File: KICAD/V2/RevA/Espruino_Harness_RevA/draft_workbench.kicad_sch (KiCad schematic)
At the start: 0 parts

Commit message: Implement Target Interface and GPIO loopback
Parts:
- added J900: TARGET INTERFACE CONNECTOR A, symbol Espruino_Harness_RevA:Target_Interface_2x12_Odd_Even
- added J901: TARGET INTERFACE CONNECTOR B, symbol Espruino_Harness_RevA:Target_Interface_2x12_Odd_Even
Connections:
- new net R0: J900.3 (Contact_03)
- new net R1: J900.4 (Contact_04)
- new net R2: J900.5 (Contact_05)
- new net R3: J900.6 (Contact_06)
- new net R4: J900.7 (Contact_07)
- new net R5: J900.9 (Contact_09)
- new net R6: J900.10 (Contact_10)
- new net TI_ANALOG_ADC_IN: J900.22 (Contact_22)
- new net TI_ANALOG_PWM_OUT: J900.21 (Contact_21)
- new net TI_BOOT_REQUEST: J900.13 (Contact_13)
- new net TI_GND: J900.12 (Contact_12), J900.16 (Contact_16), J900.2 (Contact_02), J900.20 (Contact_20), J900.24 (Contact_24), J900.8 (Contact_08), J901.12 (Contact_12), J901.16 (Contact_16), J901.2 (Contact_02), J901.20 (Contact_20), J901.24 (Contact_24), J901.8 (Contact_08)
- new net TI_GPIO_LOOP_A_IN: J901.4 (Contact_04)
- new net TI_GPIO_LOOP_A_OUT: J901.3 (Contact_03)
- new net TI_GPIO_LOOP_B_IN: J901.6 (Contact_06)
- new net TI_GPIO_LOOP_B_OUT: J901.5 (Contact_05)
- new net TI_I2C_FB: J900.18 (Contact_18)
- new net TI_I2C_INT: J900.19 (Contact_19)
- new net TI_I2C_SCL: J900.17 (Contact_17)
- new net TI_I2C_SDA: J900.15 (Contact_15)
- new net TI_ONEWIRE_DQ: J901.14 (Contact_14)
- new net TI_ONEWIRE_GPIO_A_FB: J901.15 (Contact_15)
- new net TI_ONEWIRE_GPIO_B_FB: J901.17 (Contact_17)
- new net TI_RGB_DATA: J900.14 (Contact_14)
- new net TI_SPI_CS_ADC: J901.11 (Contact_11)
- new net TI_SPI_CS_EXT: J901.13 (Contact_13)
- new net TI_SPI_MISO: J901.10 (Contact_10)
- new net TI_SPI_MOSI: J901.9 (Contact_09)
- new net TI_SPI_SCK: J901.7 (Contact_07)
- new net TI_SWITCHED_TARGET_5V: J900.23 (Contact_23), J901.23 (Contact_23)
- new net TI_TARGET_3V3: J900.1 (Contact_01), J901.1 (Contact_01)
- new net TI_TARGET_RESET_N: J900.11 (Contact_11)
- new net TI_UART_A_RX: J901.19 (Contact_19)
- new net TI_UART_A_TX: J901.18 (Contact_18)
- new net TI_UART_B_RX: J901.22 (Contact_22)
- new net TI_UART_B_TX: J901.21 (Contact_21)

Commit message: Implement V2 routing fabric and control
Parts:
- added C610, C611: 100nF, Capacitor_SMD:C_0603_1608Metric, symbol Device:C
- added JP610: A0 default 1, Jumper:SolderJumper-3_P1.3mm_Bridged12_RoundedPad1.0x1.5mm_NumberLabels, symbol Jumper:SolderJumper_3_Bridged12
- added JP611: A1 default 0, Jumper:SolderJumper-3_P1.3mm_Bridged12_RoundedPad1.0x1.5mm_NumberLabels, symbol Jumper:SolderJumper_3_Bridged12
- added JP612, JP615: A2 default 0, Jumper:SolderJumper-3_P1.3mm_Bridged12_RoundedPad1.0x1.5mm_NumberLabels, symbol Jumper:SolderJumper_3_Bridged12
- added JP613: A0 default 0, Jumper:SolderJumper-3_P1.3mm_Bridged12_RoundedPad1.0x1.5mm_NumberLabels, symbol Jumper:SolderJumper_3_Bridged12
- added JP614: A1 default 1, Jumper:SolderJumper-3_P1.3mm_Bridged12_RoundedPad1.0x1.5mm_NumberLabels, symbol Jumper:SolderJumper_3_Bridged12
- added U610: MCP23017-E/SO RCTRL0, Package_SO:SOIC-28W_7.5x17.9mm_P1.27mm, symbol Espruino_Harness_RevA:MCP23017_SO
- added U611: MCP23017-E/SO RCTRL1, Package_SO:SOIC-28W_7.5x17.9mm_P1.27mm, symbol Espruino_Harness_RevA:MCP23017_SO
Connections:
- net TI_GND: now also C610.2, C611.2, JP610.3 (B), JP611.1 (A), JP612.1 (A), JP613.1 (A), JP614.3 (B), JP615.1 (A), U610.10 (VSS), U611.10 (VSS)
- new net: JP612.2 (C), U610.17 (A2)
- new net: JP615.2 (C), U611.17 (A2)
- new net: JP611.2 (C), U610.16 (A1)
- new net: JP614.2 (C), U611.16 (A1)
- new net: JP610.2 (C), U610.15 (A0)
- new net: JP613.2 (C), U611.15 (A0)
- new net ROUTE_CLEAR_N: U610.18 (~{RESET}), U611.18 (~{RESET})
- new net ROUTE_I2C_SCL: U610.12 (SCL), U611.12 (SCL)
- new net ROUTE_I2C_SDA: U610.13 (SDA), U611.13 (SDA)
- new net ROUTING_LOGIC_3V3: C610.1, C611.1, JP610.1 (A), JP611.3 (B), JP612.3 (B), JP613.3 (B), JP614.1 (A), JP615.3 (B), U610.9 (VDD), U611.9 (VDD)
- new net RP01_EN: U610.21 (GPA0)
- new net RP02_EN: U610.22 (GPA1)
- new net RP03_EN: U610.23 (GPA2)
- new net RP04_EN: U610.24 (GPA3)
- new net RP05_EN: U610.25 (GPA4)
- new net RP06_EN: U610.26 (GPA5)
- new net RP07_EN: U610.27 (GPA6)
- new net RP08_EN: U610.28 (GPA7)
- new net RP09_EN: U610.1 (GPB0)
- new net RP10_EN: U610.2 (GPB1)
- new net RP11_EN: U610.3 (GPB2)
- new net RP12_EN: U610.4 (GPB3)
- new net RP13_EN: U610.5 (GPB4)
- new net RP14_EN: U610.6 (GPB5)
- new net RP15_EN: U610.7 (GPB6)
- new net RP16_EN: U610.8 (GPB7)
- new net RP17_EN: U611.21 (GPA0)
- new net RP18_EN: U611.22 (GPA1)
- new net RP19_EN: U611.23 (GPA2)
- new net UP01_EN: U611.24 (GPA3)
- new net UP02_EN: U611.25 (GPA4)
- new net UP03_EN: U611.26 (GPA5)
- new net UP04_EN: U611.27 (GPA6)
- no-connect marks 0 -> 13
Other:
- note added: "Address selectors: pads 1-2 are default; to change, cut 1-2 and bridge 2-3. Never bridge both."
- note added: "Both controllers share ROUTE_I2C_SDA / ROUTE_I2C_SCL and active-low ROUTE_CLEAR_N"
- note added: "ROUTING CONTROLLER DRAFT â€” REVIEW BEFORE COPYING TO PRODUCTION"
- note added: "U610 â€” RCTRL0 â€” MCP23017 address 0x21"
- note added: "U611 â€” RCTRL1 â€” MCP23017 address 0x22"

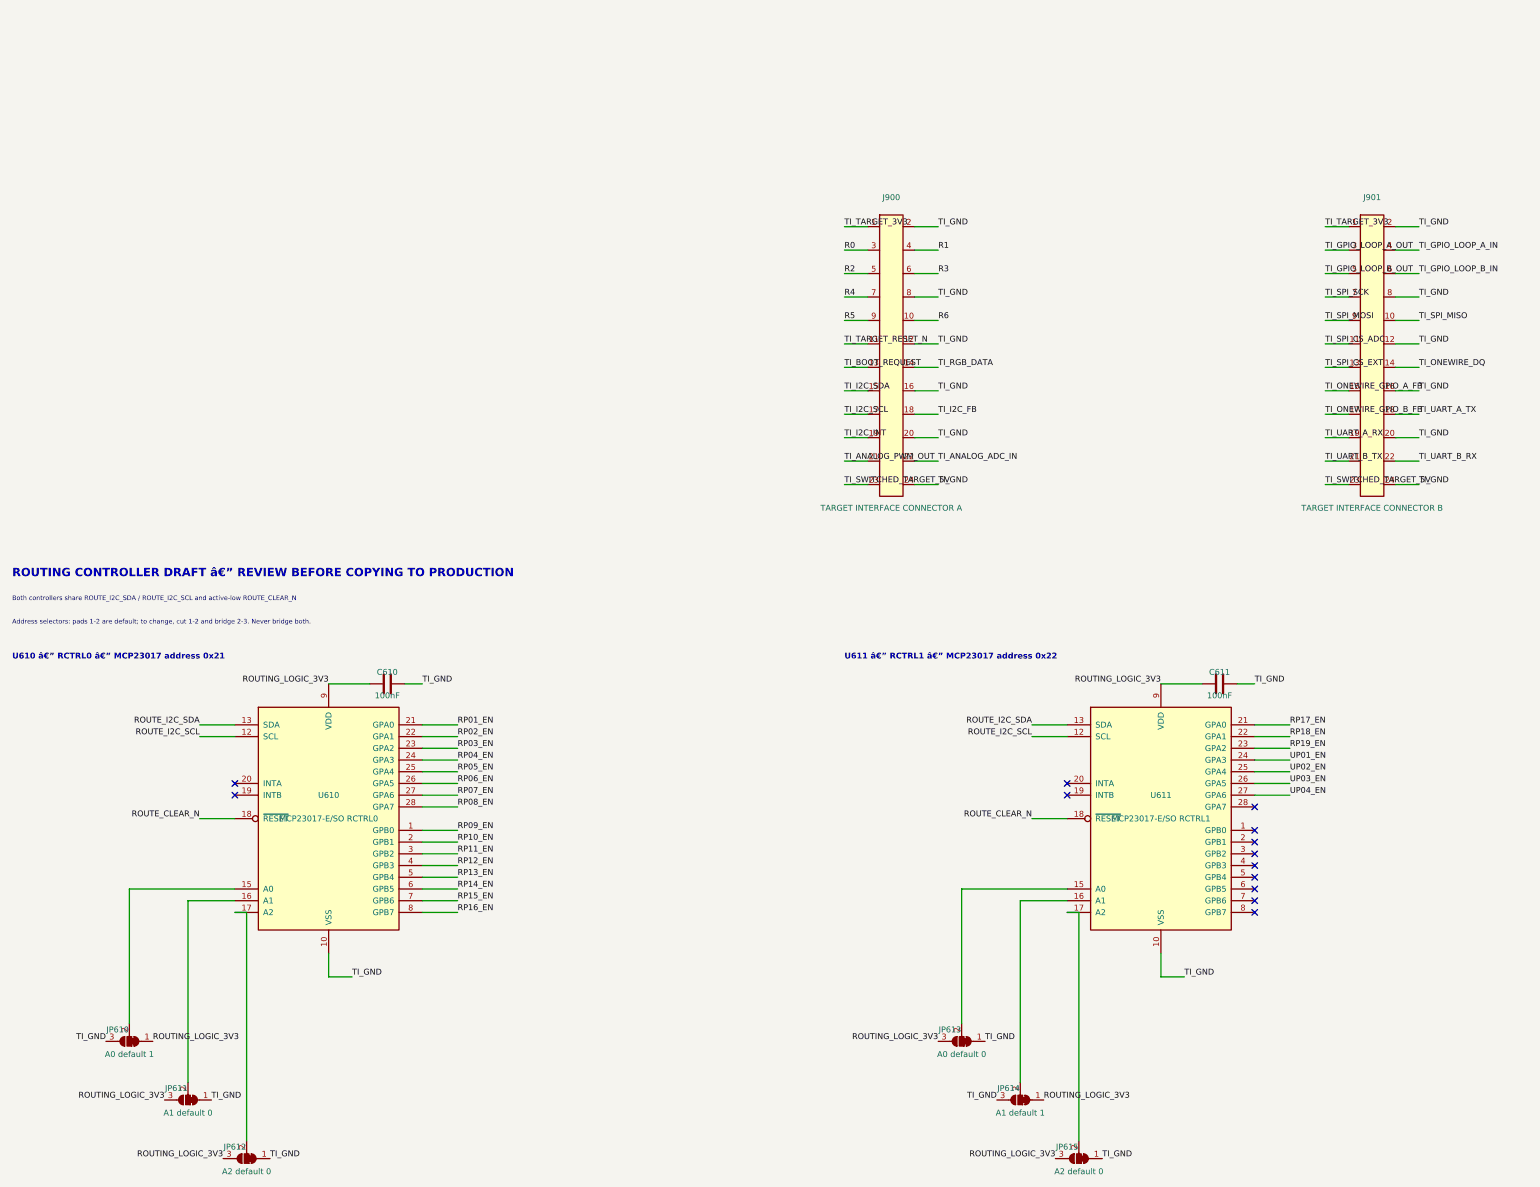
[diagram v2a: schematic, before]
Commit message: Implement Rev-A power control service draft
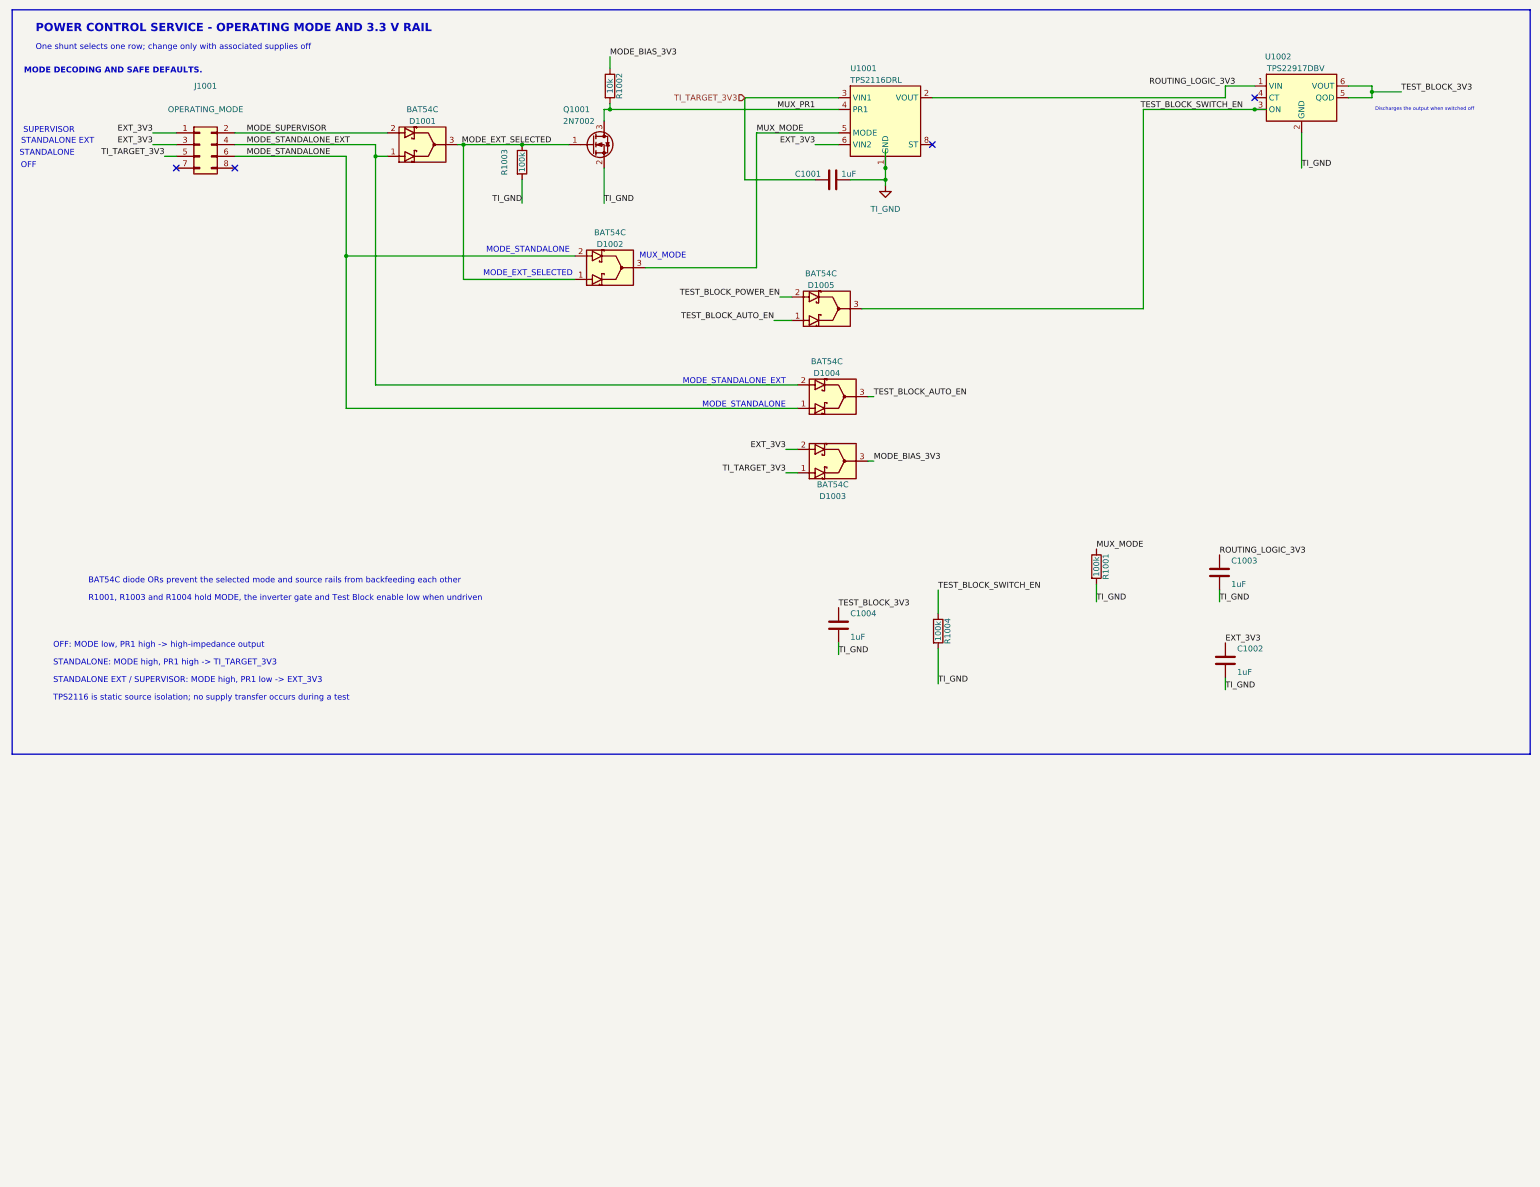
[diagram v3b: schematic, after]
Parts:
- removed C610, C611: 100nF, Capacitor_SMD:C_0603_1608Metric, symbol Device:C
- removed J900: TARGET INTERFACE CONNECTOR A, symbol Espruino_Harness_RevA:Target_Interface_2x12_Odd_Even
- removed J901: TARGET INTERFACE CONNECTOR B, symbol Espruino_Harness_RevA:Target_Interface_2x12_Odd_Even
- removed JP610: A0 default 1, Jumper:SolderJumper-3_P1.3mm_Bridged12_RoundedPad1.0x1.5mm_NumberLabels, symbol Jumper:SolderJumper_3_Bridged12
- removed JP611: A1 default 0, Jumper:SolderJumper-3_P1.3mm_Bridged12_RoundedPad1.0x1.5mm_NumberLabels, symbol Jumper:SolderJumper_3_Bridged12
- removed JP612, JP615: A2 default 0, Jumper:SolderJumper-3_P1.3mm_Bridged12_RoundedPad1.0x1.5mm_NumberLabels, symbol Jumper:SolderJumper_3_Bridged12
- removed JP613: A0 default 0, Jumper:SolderJumper-3_P1.3mm_Bridged12_RoundedPad1.0x1.5mm_NumberLabels, symbol Jumper:SolderJumper_3_Bridged12
- removed JP614: A1 default 1, Jumper:SolderJumper-3_P1.3mm_Bridged12_RoundedPad1.0x1.5mm_NumberLabels, symbol Jumper:SolderJumper_3_Bridged12
- removed U610: MCP23017-E/SO RCTRL0, Package_SO:SOIC-28W_7.5x17.9mm_P1.27mm, symbol Espruino_Harness_RevA:MCP23017_SO
- removed U611: MCP23017-E/SO RCTRL1, Package_SO:SOIC-28W_7.5x17.9mm_P1.27mm, symbol Espruino_Harness_RevA:MCP23017_SO
- added C1001, C1002, C1003, C1004: 1uF, Capacitor_SMD:C_0603_1608Metric, symbol Device:C
- added D1001, D1002, D1003, D1004, D1005: BAT54C, Package_TO_SOT_SMD:SOT-23, symbol Espruino_Harness_RevA:BAT54C_AAK
- added J1001: OPERATING_MODE, Connector_PinHeader_2.54mm:PinHeader_2x04_P2.54mm_Vertical, symbol Connector_Generic:Conn_02x04_Odd_Even
- added Q1001: 2N7002, Package_TO_SOT_SMD:SOT-23, symbol Espruino_Harness_RevA:NMOS_2N7002_GSD
- added R1001, R1003, R1004: 100k, Resistor_SMD:R_0603_1608Metric, symbol Device:R
- added R1002: 10k, Resistor_SMD:R_0603_1608Metric, symbol Device:R
- added U1001: TPS2116DRL, Package_TO_SOT_SMD:SOT-583-8, symbol Power_Management:TPS2116DRL
- added U1002: TPS22917DBV, Package_TO_SOT_SMD:SOT-23-6, symbol Power_Management:TPS22917DBV
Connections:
- net ROUTING_LOGIC_3V3: now also C1003.1
- net TI_GND: now also C1001.2, C1002.2, C1003.2, C1004.2, Q1001.2 (S), R1001.2, R1003.2, R1004.2, U1001.1 (GND), U1002.2 (GND)
- net TI_TARGET_3V3: now also C1001.1, D1003.1 (A1), J1001.5 (Pin_5), U1001.3 (VIN1)
- new net: U1001.2 (VOUT), U1001.7 (VOUT), U1002.1 (VIN)
- new net EXT_3V3: C1002.1, D1003.2 (A2), J1001.1 (Pin_1), J1001.3 (Pin_3), U1001.6 (VIN2)
- new net MODE_BIAS_3V3: D1003.3 (K), R1002.1
- new net MODE_EXT_SELECTED: D1001.3 (K), D1002.1 (A1), Q1001.1 (G), R1003.1
- new net MODE_STANDALONE: D1002.2 (A2), D1004.1 (A1), J1001.6 (Pin_6)
- new net MODE_STANDALONE_EXT: D1001.1 (A1), D1004.2 (A2), J1001.4 (Pin_4)
- new net MODE_SUPERVISOR: D1001.2 (A2), J1001.2 (Pin_2)
- new net MUX_MODE: D1002.3 (K), R1001.1, U1001.5 (MODE)
- new net MUX_PR1: Q1001.3 (D), R1002.2, U1001.4 (PR1)
- new net TEST_BLOCK_3V3: C1004.1, U1002.5 (QOD), U1002.6 (VOUT)
- new net TEST_BLOCK_AUTO_EN: D1004.3 (K), D1005.1 (A1)
- new net TEST_BLOCK_POWER_EN: D1005.2 (A2)
- new net TEST_BLOCK_SWITCH_EN: D1005.3 (K), R1004.1, U1002.3 (ON)
- no-connect marks 13 -> 4
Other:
- note added: "BAT54C diode ORs prevent the selected mode and source rails from backfeeding each other"
- note added: "Discharges the output when switched off"
- note added: "MODE DECODING AND SAFE DEFAULTS."
- note added: "MODE_EXT_SELECTED"
- note added: "MODE_STANDALONE"
- note added: "MODE_STANDALONE_EXT"
- note added: "MUX_MODE"
- note added: "OFF"
- note added: "OFF: MODE low, PR1 high -> high-impedance output"
- note added: "One shunt selects one row; change only with associated supplies off"
- note added: "POWER CONTROL SERVICE - OPERATING MODE AND 3.3 V RAIL"
- note added: "R1001, R1003 and R1004 hold MODE, the inverter gate and Test Block enable low when undriven"
- note added: "STANDALONE"
- note added: "STANDALONE EXT"
- note added: "STANDALONE EXT / SUPERVISOR: MODE high, PR1 low -> EXT_3V3"
- note added: "STANDALONE: MODE high, PR1 high -> TI_TARGET_3V3"
- note added: "SUPERVISOR"
- note added: "TPS2116 is static source isolation; no supply transfer occurs during a test"
- note removed: "Address selectors: pads 1-2 are default; to change, cut 1-2 and bridge 2-3. Never bridge both."
- note removed: "Both controllers share ROUTE_I2C_SDA / ROUTE_I2C_SCL and active-low ROUTE_CLEAR_N"
- note removed: "ROUTING CONTROLLER DRAFT â€” REVIEW BEFORE COPYING TO PRODUCTION"
- note removed: "U610 â€” RCTRL0 â€” MCP23017 address 0x21"
- note removed: "U611 â€” RCTRL1 â€” MCP23017 address 0x22"
